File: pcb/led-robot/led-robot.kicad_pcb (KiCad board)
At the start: 2 copper layers, 33.3 x 31.2 mm, 30 parts, among them J1 data, U1 MAX7219

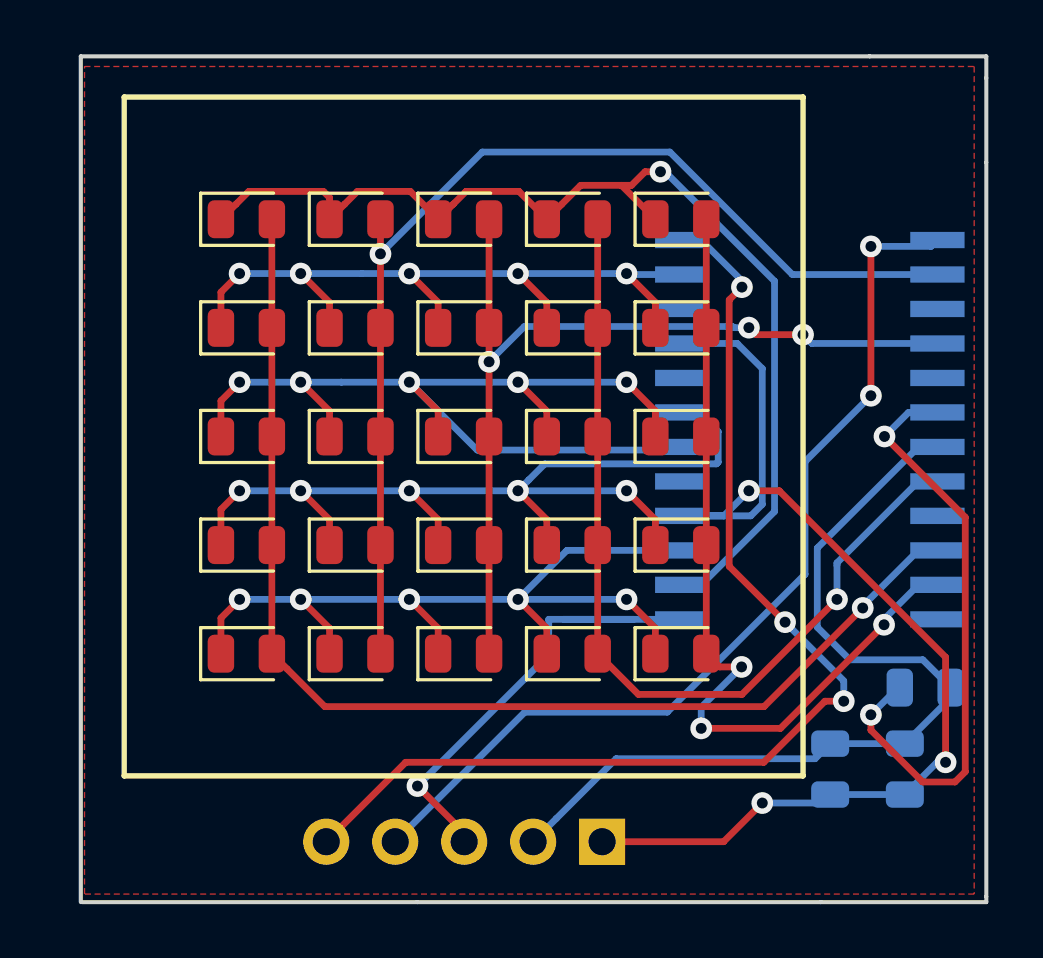
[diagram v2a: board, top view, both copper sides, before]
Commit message: make the pcb a litter bigger
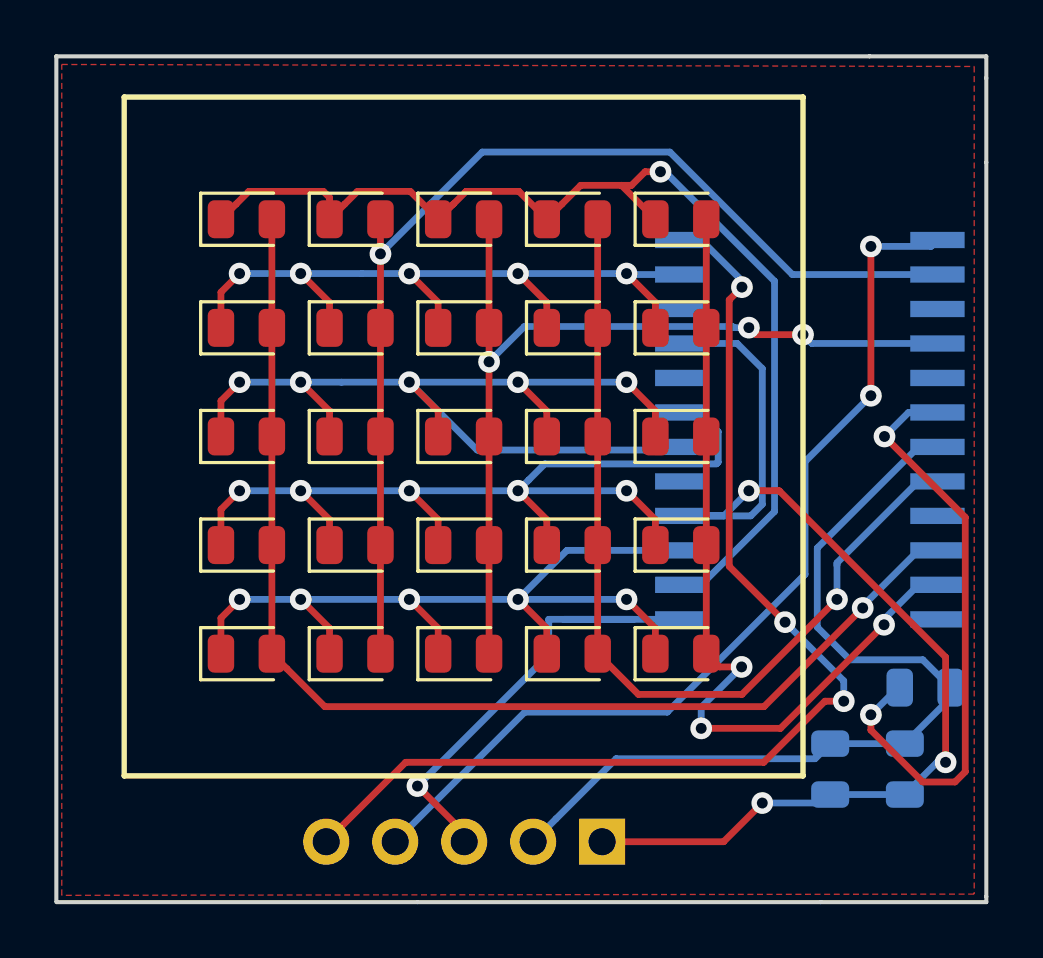
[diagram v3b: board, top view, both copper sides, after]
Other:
- board size 33.3 x 31.2 mm -> 34.2 x 31.2 mm
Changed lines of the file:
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@@
   (gr_line (start 204.15 102.15) (end 210.25 102.15) (layer Edge.Cuts) (width 0.15))
   (gr_line (start 189.3 102.15) (end 204.15 102.15) (layer Edge.Cuts) (width 0.15))
-  (gr_line (start 176.95 102.15) (end 189.3 102.15) (layer Edge.Cuts) (width 0.15))
-  (gr_line (start 176.9 71) (end 176.9 102.15) (layer Edge.Cuts) (width 0.15))
-  (gr_line (start 205.95 71) (end 176.9 71) (layer Edge.Cuts) (width 0.15))
+  (gr_line (start 176 102.15) (end 189.3 102.15) (layer Edge.Cuts) (width 0.15))
+  (gr_line (start 176 71) (end 176 102.1) (layer Edge.Cuts) (width 0.15))
+  (gr_line (start 205.95 71) (end 176 71) (layer Edge.Cuts) (width 0.15))
   (gr_line (start 210.25 71) (end 205.95 71) (layer Edge.Cuts) (width 0.15))
   (gr_line (start 203.5 97.5) (end 203.5 72.5) (layer F.SilkS) (width 0.2))
@@
     (polygon
       (pts
-        (xy 209.804 71.374) (xy 209.804 101.854) (xy 177.038 101.854) (xy 177.038 71.374)
+        (xy 209.804 71.374) (xy 209.804 101.854) (xy 176.2 101.9) (xy 176.2 71.3)
       )
     )
